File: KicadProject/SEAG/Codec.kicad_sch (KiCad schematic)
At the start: 7 parts, among them U3 SGTL5000XNAA3

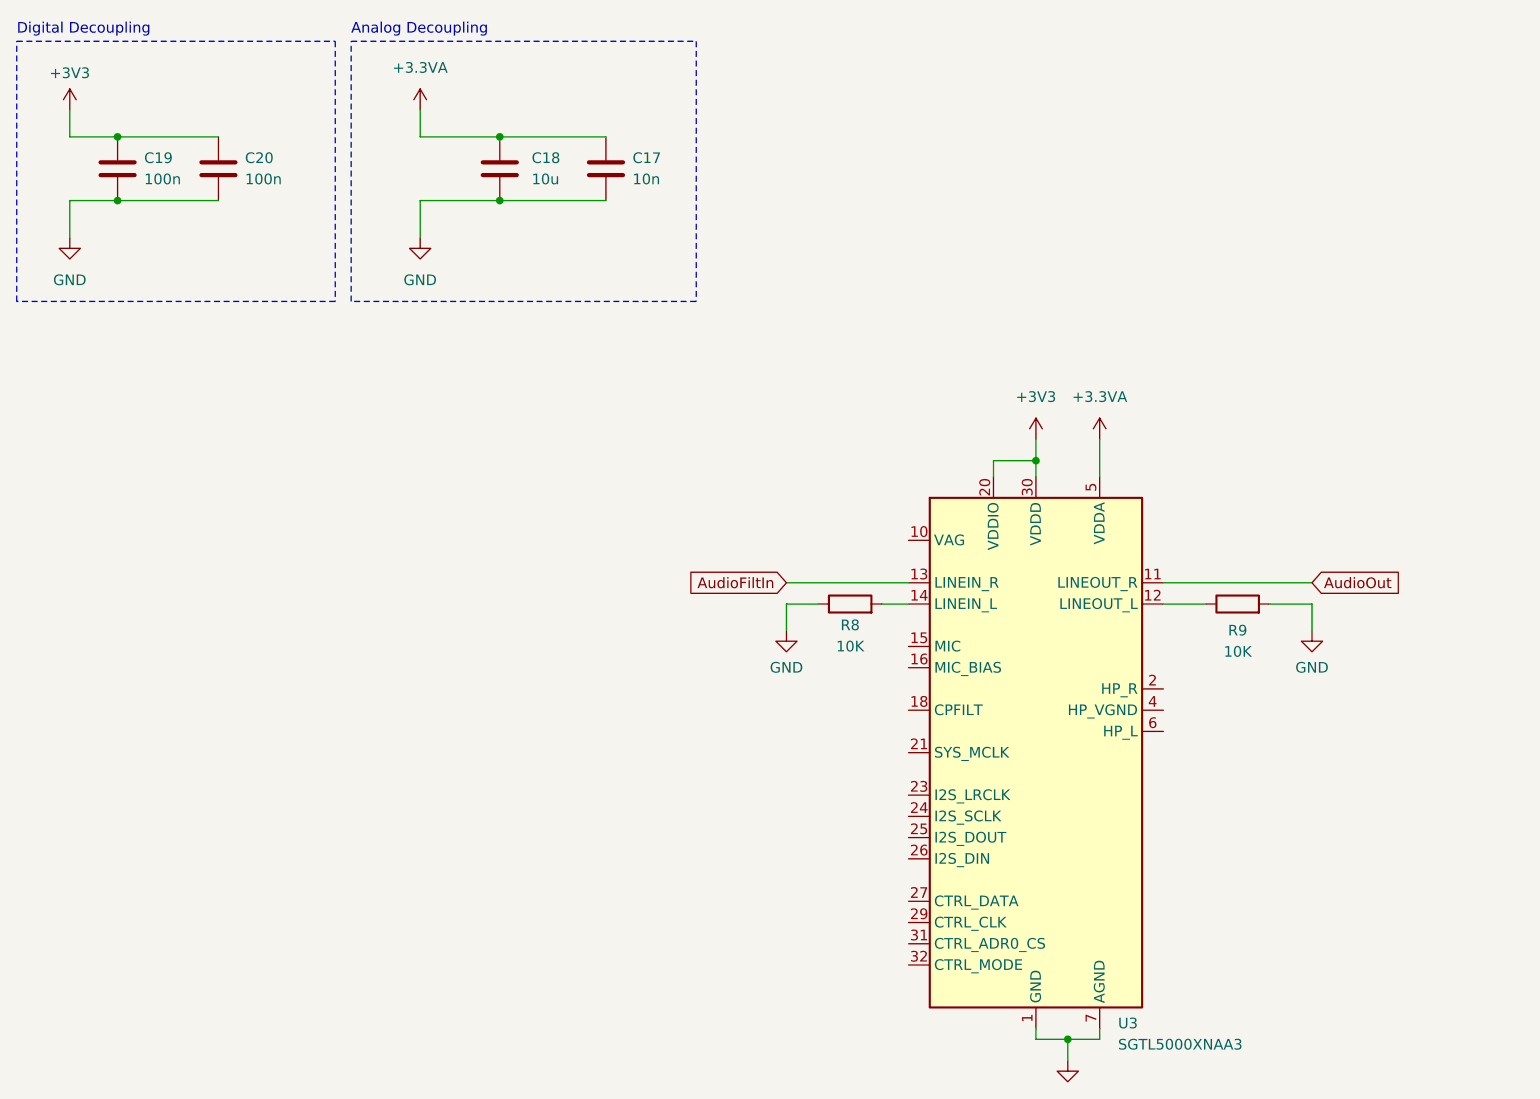
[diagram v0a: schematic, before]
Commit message: Finished PCB, stil uncertain about couple things
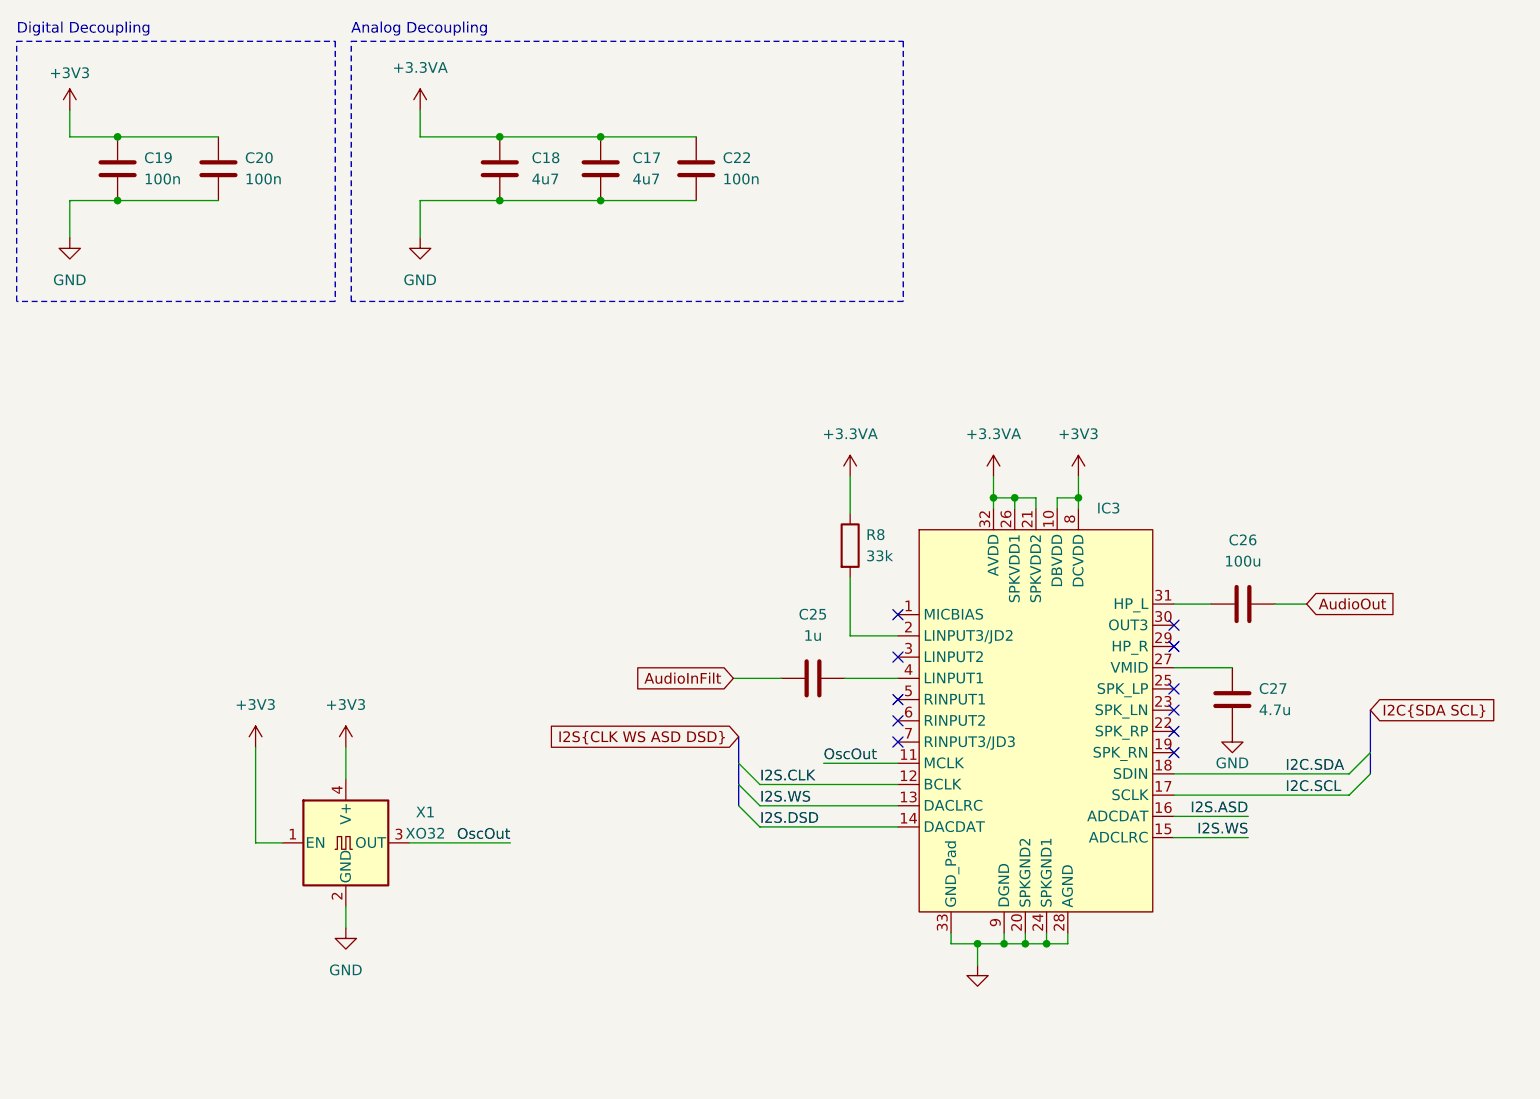
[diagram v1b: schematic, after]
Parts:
- removed R9: 10K, Resistor_SMD:R_0805_2012Metric, symbol Device:R
- removed U3: SGTL5000XNAA3, Package_DFN_QFN:QFN-32-1EP_5x5mm_P0.5mm_EP3.6x3.6mm, symbol Audio:SGTL5000XNAA3
- added C22: 100n, Capacitor_SMD:C_0805_2012Metric, symbol Device:C
- added C25: 1u, Capacitor_SMD:C_0805_2012Metric, symbol Device:C
- added C26: 100u, Capacitor_SMD:C_0805_2012Metric, symbol Device:C
- added C27: 4.7u, Capacitor_SMD:C_0805_2012Metric, symbol Device:C
- added IC3: ~, SamacSys_Parts:QFN50P500X500X100-33N, symbol MyLibrary:WM8960
- added X1: XO32, Oscillator:Oscillator_SMD_EuroQuartz_XO32-4Pin_3.2x2.5mm, symbol Oscillator:XO32
- C17: value 10n -> 4u7
- C18: value 10u -> 4u7
- R8: value 10K -> 33k
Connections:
- net +3.3VA: now also R8.1, C22.1, IC3.21 (SPKVDD2), IC3.26 (SPKVDD1), IC3.32 (AVDD)
- net +3V3: now also IC3.10 (DBVDD), IC3.8 (DCVDD), X1.1 (EN), X1.4 (V+)
- net AudioOut: now also C26.2
- net GND: now also C22.2, C27.2, IC3.20 (SPKGND2), IC3.24 (SPKGND1), IC3.28 (AGND), IC3.33 (GND_Pad), IC3.9 (DGND), X1.2 (GND); no longer R8.1
- net at R8.2: now also IC3.2 (LINPUT3/JD2)
- new net: C27.1, IC3.27 (VMID)
- new net: C25.2, IC3.4 (LINPUT1)
- new net: C26.1, IC3.31 (HP_L)
- new net AudioInFilt: C25.1
- new net I2C.SCL: IC3.17 (SCLK)
- new net I2C.SDA: IC3.18 (SDIN)
- new net I2S.ASD: IC3.16 (ADCDAT)
- new net I2S.CLK: IC3.12 (BCLK)
- new net I2S.DSD: IC3.14 (DACDAT)
- new net I2S.WS: IC3.13 (DACLRC), IC3.15 (ADCLRC)
- new net OscOut: IC3.11 (MCLK), X1.3 (OUT)
- no-connect marks 0 -> 11

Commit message: PCB rev 2
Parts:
- removed X1: XO32, Oscillator:Oscillator_SMD_EuroQuartz_XO32-4Pin_3.2x2.5mm, symbol Oscillator:XO32
- renumbered C19 to C501, C20 to C502, C18 to C503, C17 to C504, C22 to C505, C25 to C506, C27 to C507, C26 to C508, R8 to R501
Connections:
- net OscOut renamed MCLK
